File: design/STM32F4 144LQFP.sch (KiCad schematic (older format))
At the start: 16 parts, among them P2 SWD, U1 STM32F40X_LQFP64, X2 8MHz 10ppm

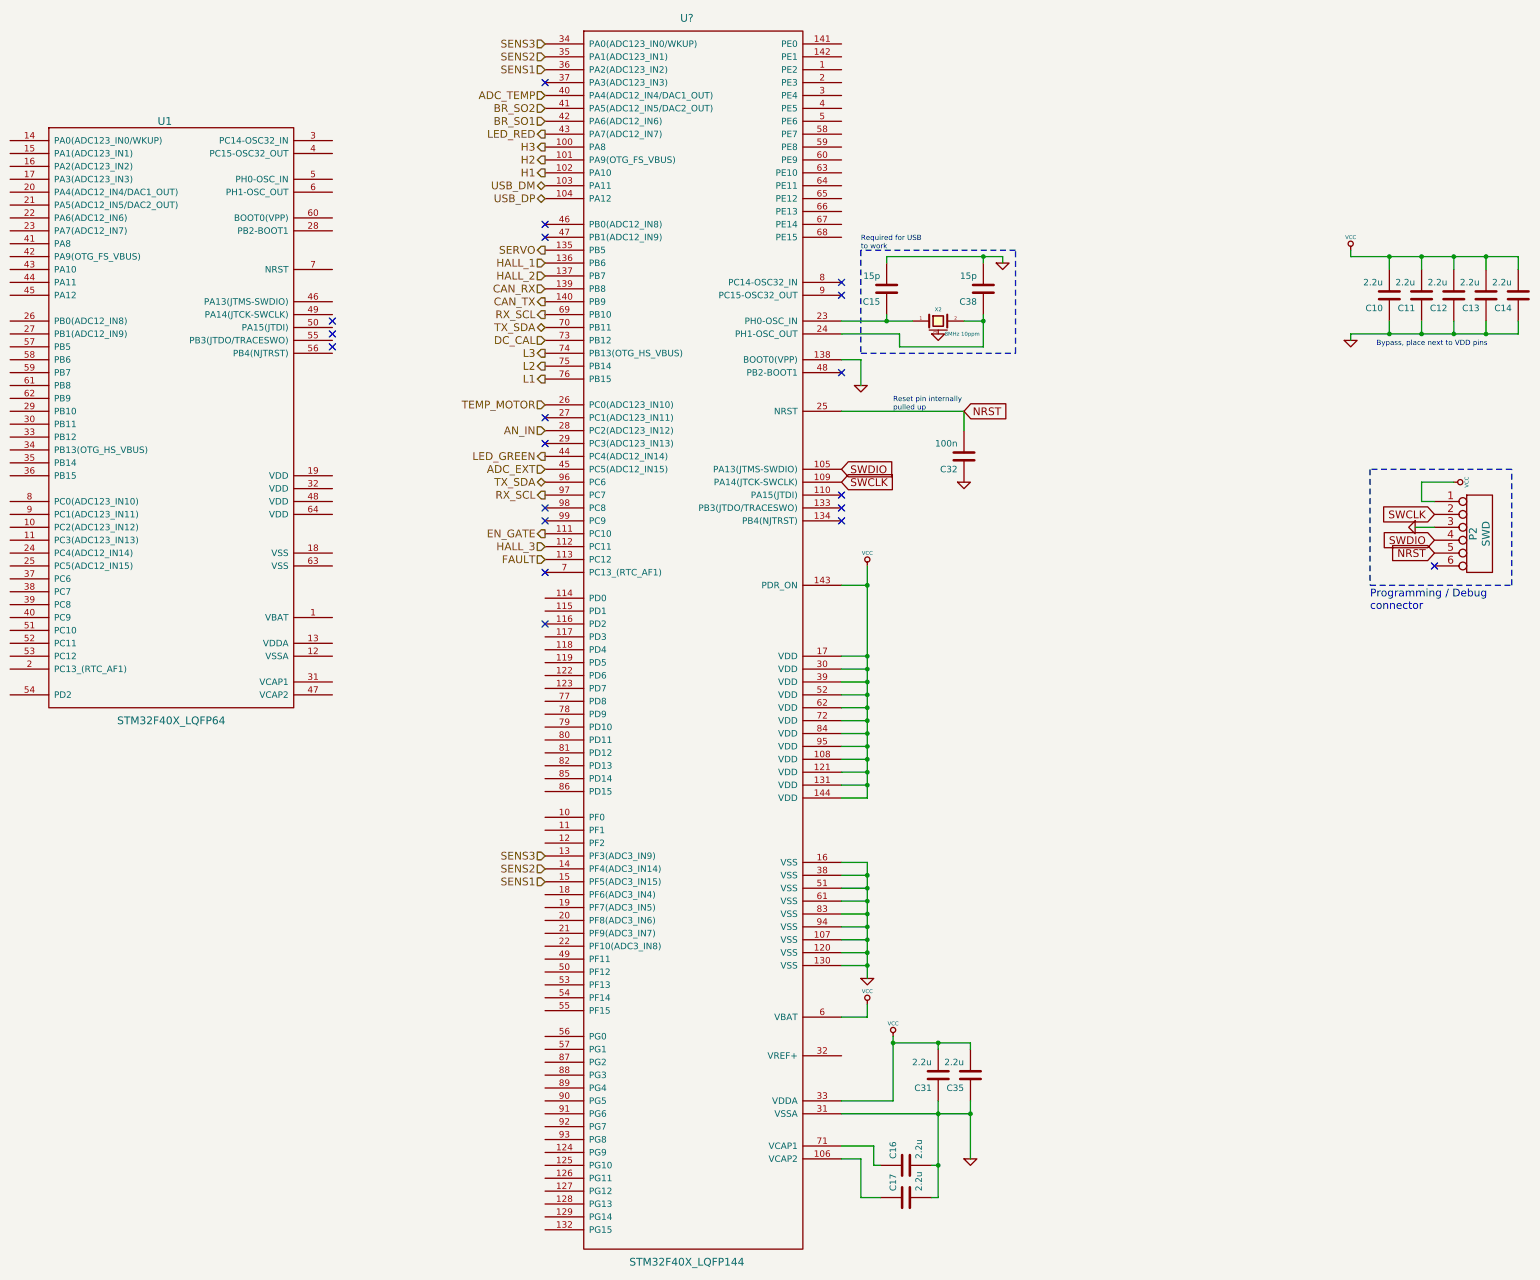
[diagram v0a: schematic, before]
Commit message: Add a electronic for second motor and add new pin's for it on MCU; TODO Add new mosfets
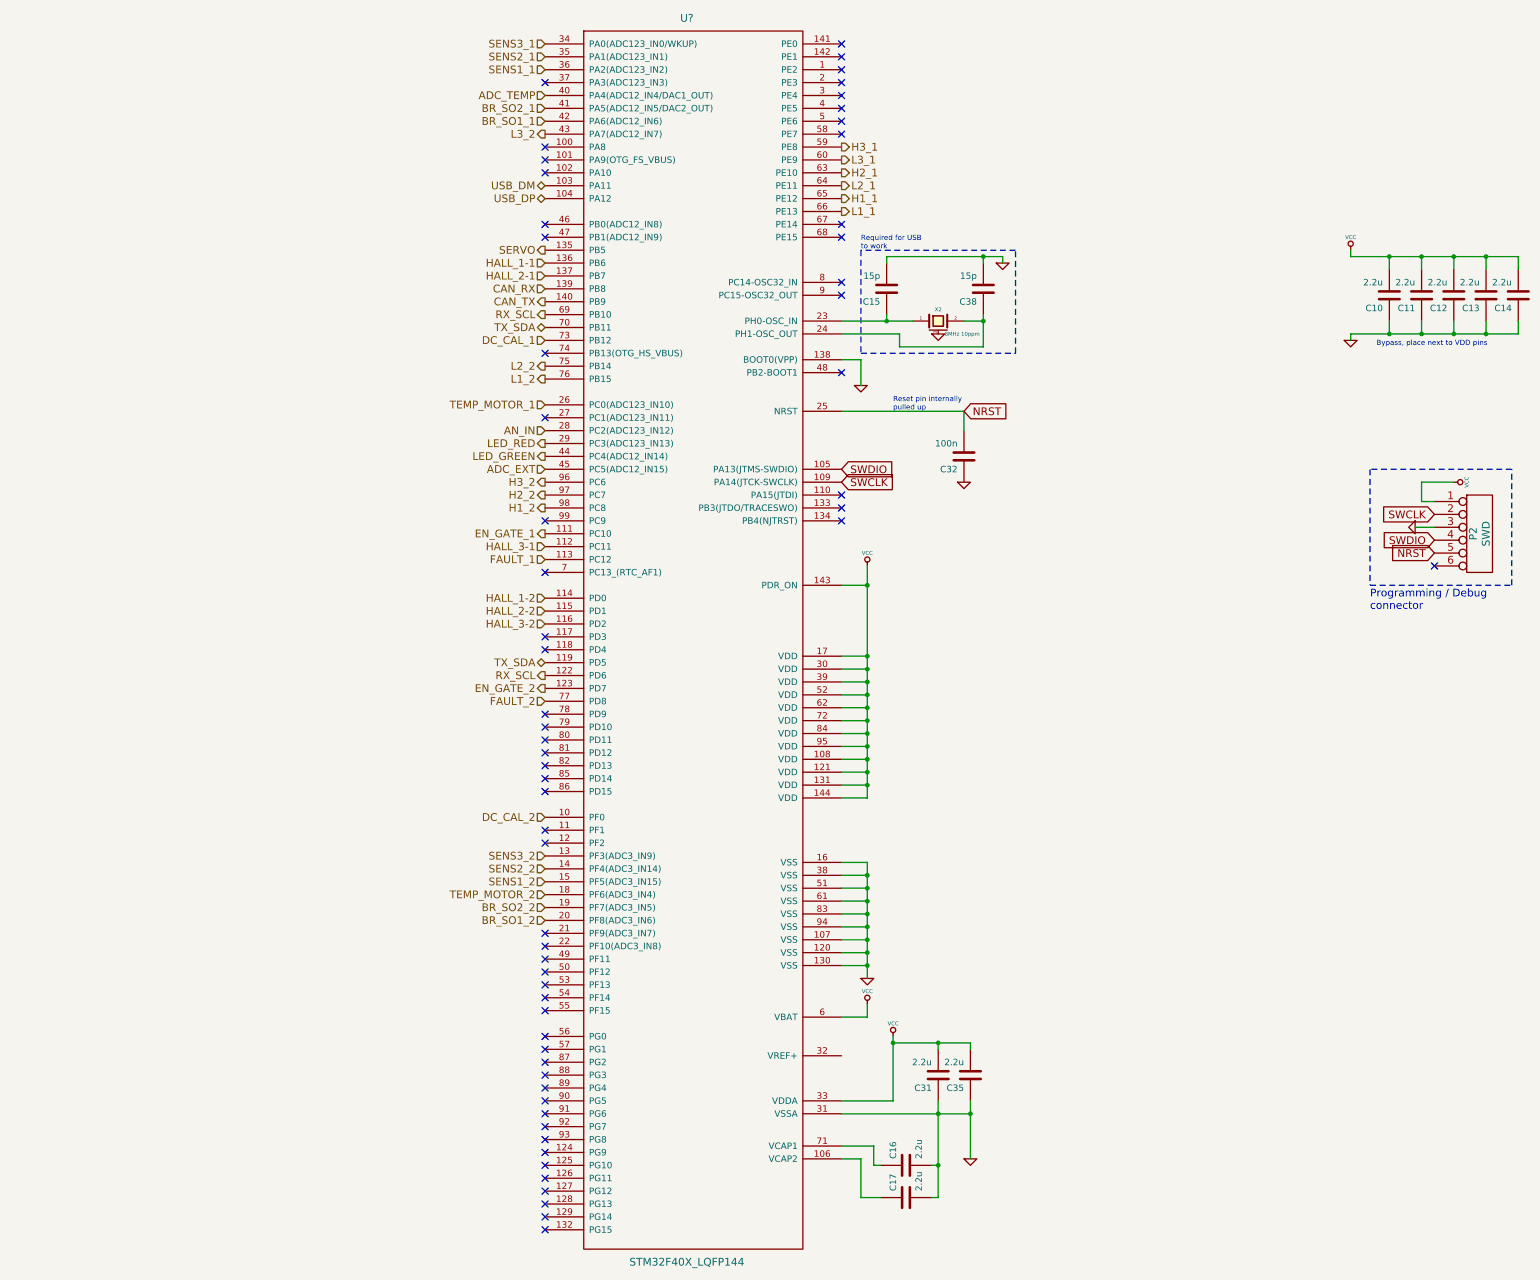
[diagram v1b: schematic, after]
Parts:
- removed U1: STM32F40X_LQFP64, CRF1:lqfp64_pad_mod, symbol STM32F40X_LQFP64
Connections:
- net LED_RED: now also U?.29 (PC3(ADC123_IN13)); no longer U?.43 (PA7(ADC12_IN7))
- net RX_SCL: now also U?.122 (PD6); no longer U?.97 (PC7)
- net TX_SDA: now also U?.119 (PD5); no longer U?.96 (PC6)
- net DC_CAL_2: now reaches U?.10 (PF0)
- net HALL_1-2: now reaches U?.114 (PD0)
- net HALL_2-2: now reaches U?.115 (PD1)
- net HALL_3-2: now reaches U?.116 (PD2)
- net EN_GATE_2: now reaches U?.123 (PD7)
- net TEMP_MOTOR_2: now reaches U?.18 (PF6(ADC3_IN4))
- net BR_SO2_2: now reaches U?.19 (PF7(ADC3_IN5))
- net BR_SO1_2: now reaches U?.20 (PF8(ADC3_IN6))
- net H3_1: now reaches U?.59 (PE8)
- net L3_1: now reaches U?.60 (PE9)
- net H2_1: now reaches U?.63 (PE10)
- net L2_1: now reaches U?.64 (PE11)
- net H1_1: now reaches U?.65 (PE12)
- net L1_1: now reaches U?.66 (PE13)
- net FAULT_2: now reaches U?.77 (PD8)
- net H1_2: now reaches U?.98 (PC8)
- net BR_SO1 renamed BR_SO1_1
- net BR_SO2 renamed BR_SO2_1
- net DC_CAL renamed DC_CAL_1
- net EN_GATE renamed EN_GATE_1
- net FAULT renamed FAULT_1
- net H1: no longer names the net of U?.102 (PA10)
- net H2: no longer names the net of U?.101 (PA9(OTG_FS_VBUS))
- net H3: no longer names the net of U?.100 (PA8)
- net HALL_1 renamed HALL_1-1
- net HALL_2 renamed HALL_2-1
- net HALL_3 renamed HALL_3-1
- net L1 renamed L1_2
- net L2 renamed L2_2
- net L3: no longer names the net of U?.74 (PB13(OTG_HS_VBUS))
- net SENS1 renamed SENS1_1
- net SENS1_1: no longer U?.15 (PF5(ADC3_IN15))
- net SENS2 renamed SENS2_1
- net SENS2_1: no longer U?.14 (PF4(ADC3_IN14))
- net SENS3 renamed SENS3_1
- net SENS3_1: no longer U?.13 (PF3(ADC3_IN9))
- net TEMP_MOTOR renamed TEMP_MOTOR_1
- new net H2_2: U?.97 (PC7)
- new net H3_2: U?.96 (PC6)
- new net L3_2: U?.43 (PA7(ADC12_IN7))
- new net SENS1_2: U?.15 (PF5(ADC3_IN15))
- new net SENS2_2: U?.14 (PF4(ADC3_IN14))
- new net SENS3_2: U?.13 (PF3(ADC3_IN9))
- no-connect marks 19 -> 61

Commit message: Make change in annotations and some small fixes
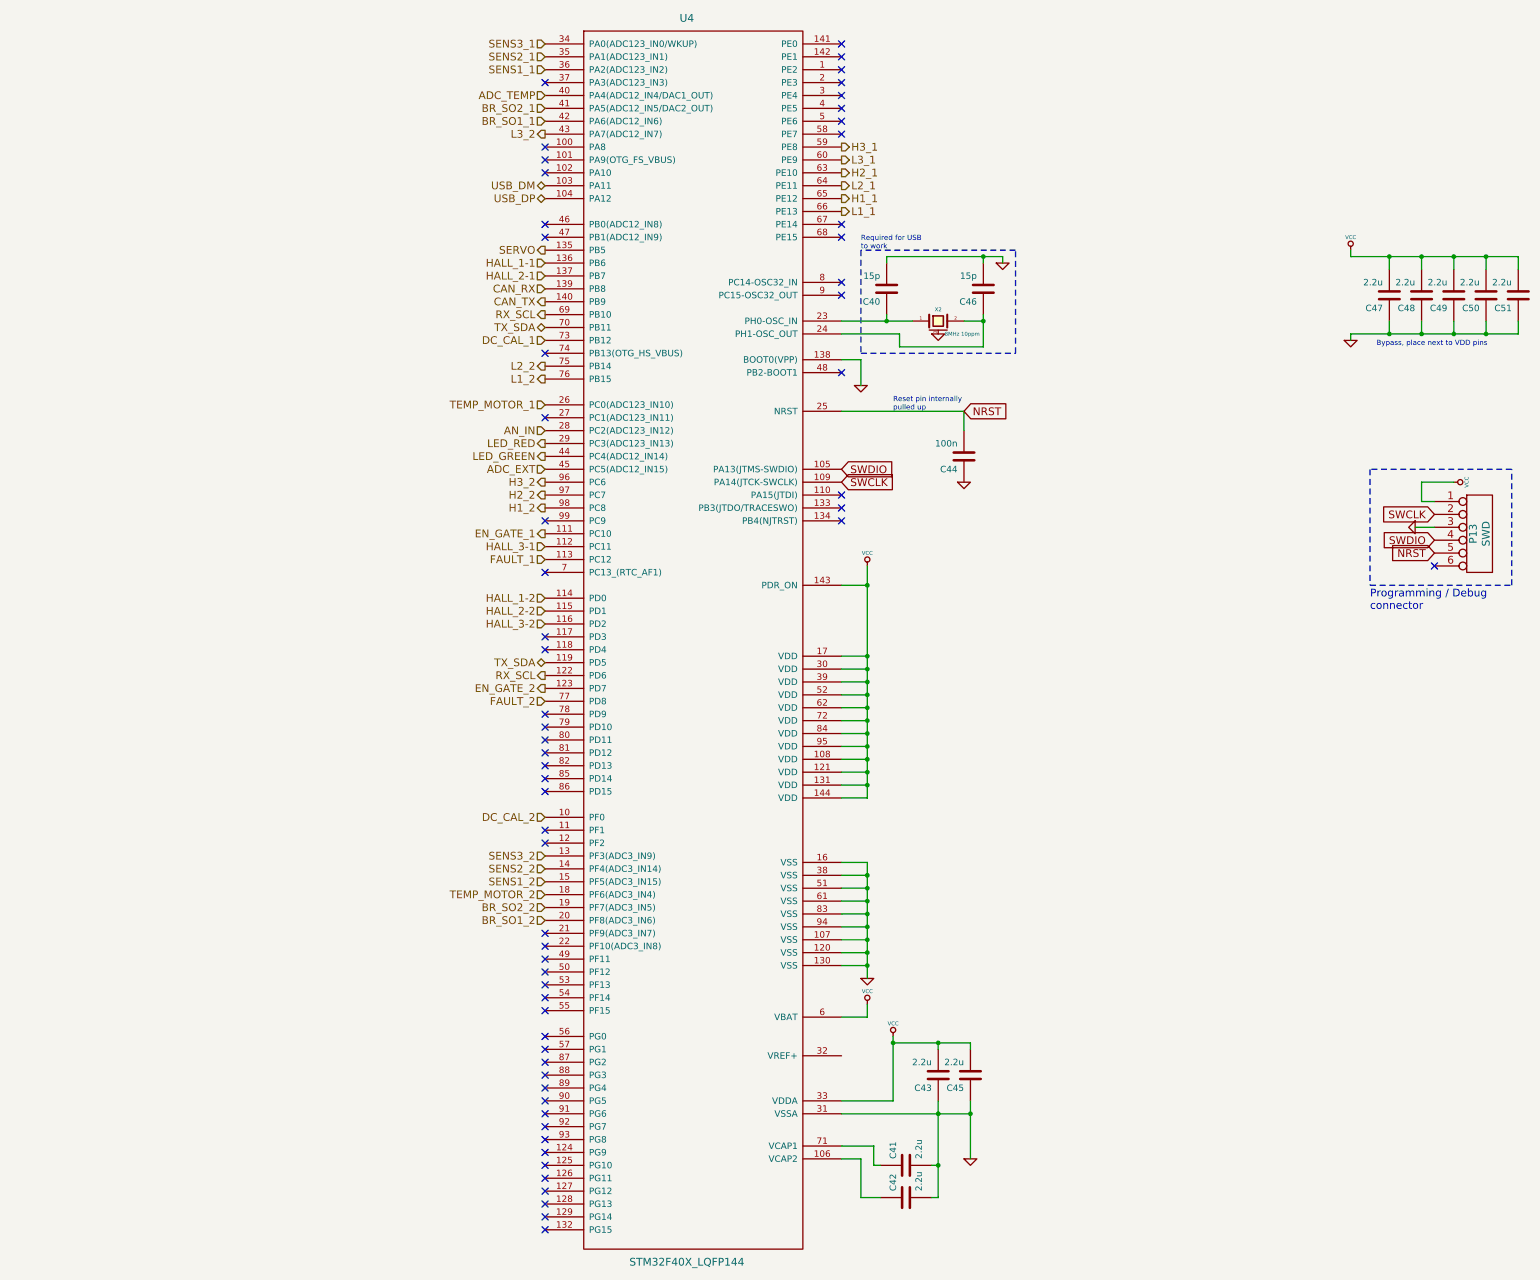
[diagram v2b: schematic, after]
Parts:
- gave numbers to parts that had none: 1
- renumbered C15 to C40, C16 to C41, C17 to C42, C31 to C43, C32 to C44, C35 to C45, C38 to C46, C10 to C47, C11 to C48, C12 to C49, C13 to C50, C14 to C51, P2 to P13
